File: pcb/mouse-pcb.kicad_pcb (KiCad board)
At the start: 2 copper layers, 47.6 x 42.5 mm, 1 part, among them U1 PAW3395-T6QU

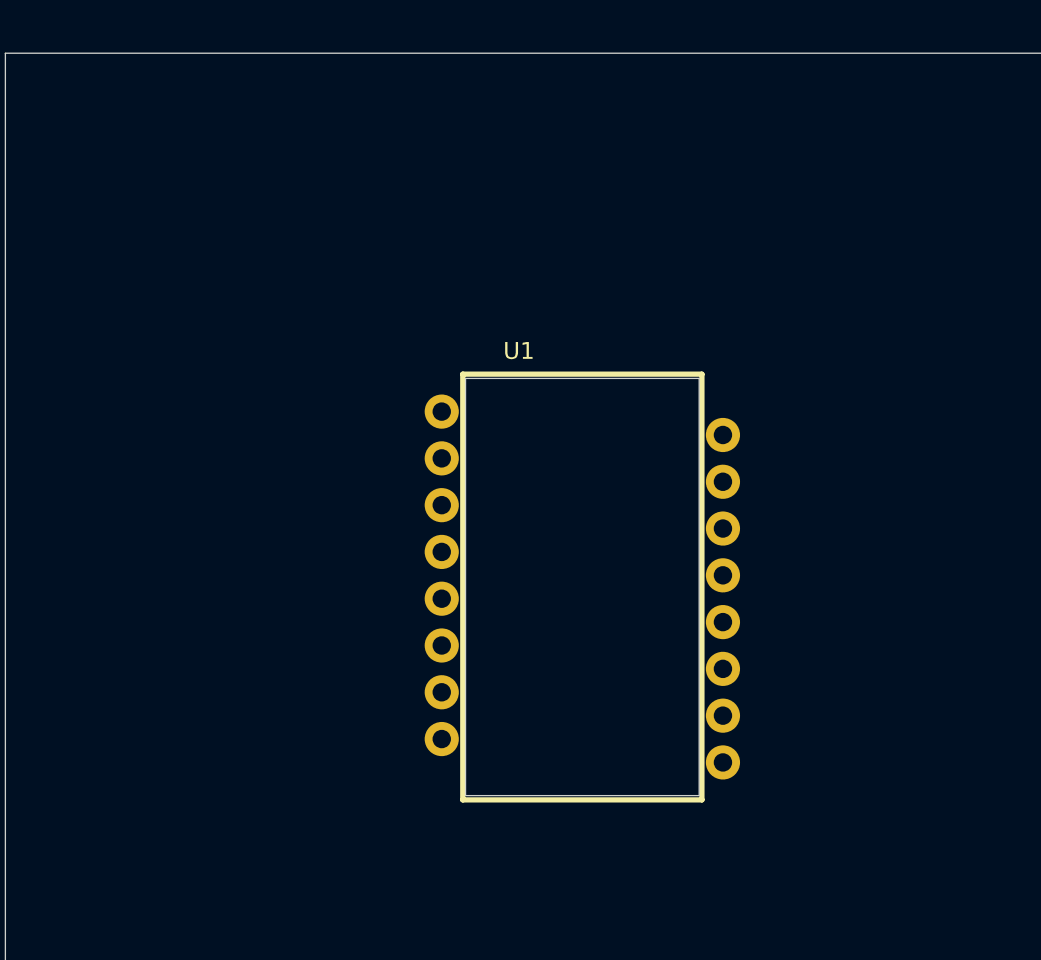
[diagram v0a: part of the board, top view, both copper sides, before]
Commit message: feat: add new library for the mouse
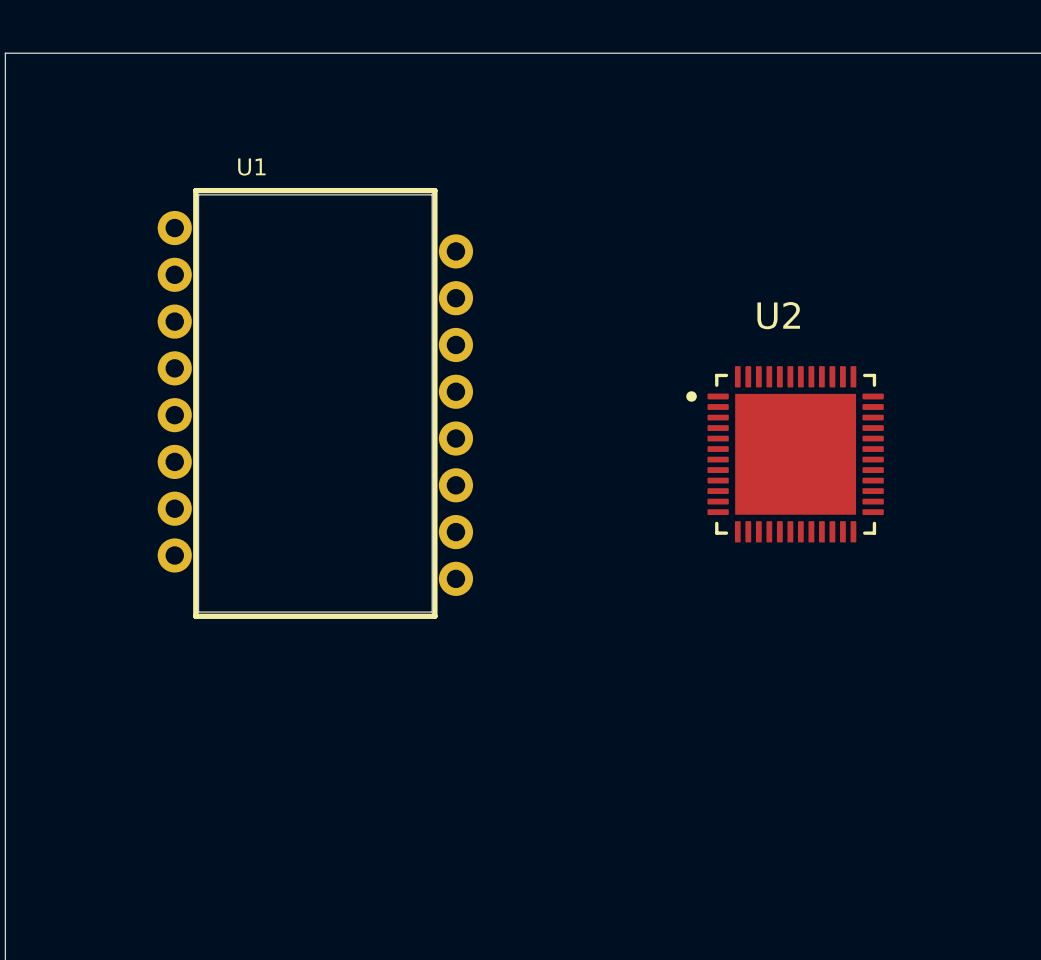
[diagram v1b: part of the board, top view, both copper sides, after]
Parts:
- added U2: NRF54L15-QFAA-R, mouse_library:QFN40P600X600X90-49N, F.Cu at (89.8, 44.8)
- U1: footprint paw3395:paw3395 -> mouse_library:paw3395
- moved U1 12.3 mm to (71.5, 42.9)
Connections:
- U1 pad 3: unconnected-(U1-GND-Pad3) -> GND
- U1 pad 4: unconnected-(U1-VDD-Pad4) -> +3V3
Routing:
- added copper zone on In2.Cu, net +3V3
- added copper zone on In1.Cu, net GND
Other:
- copper layers 2 -> 4

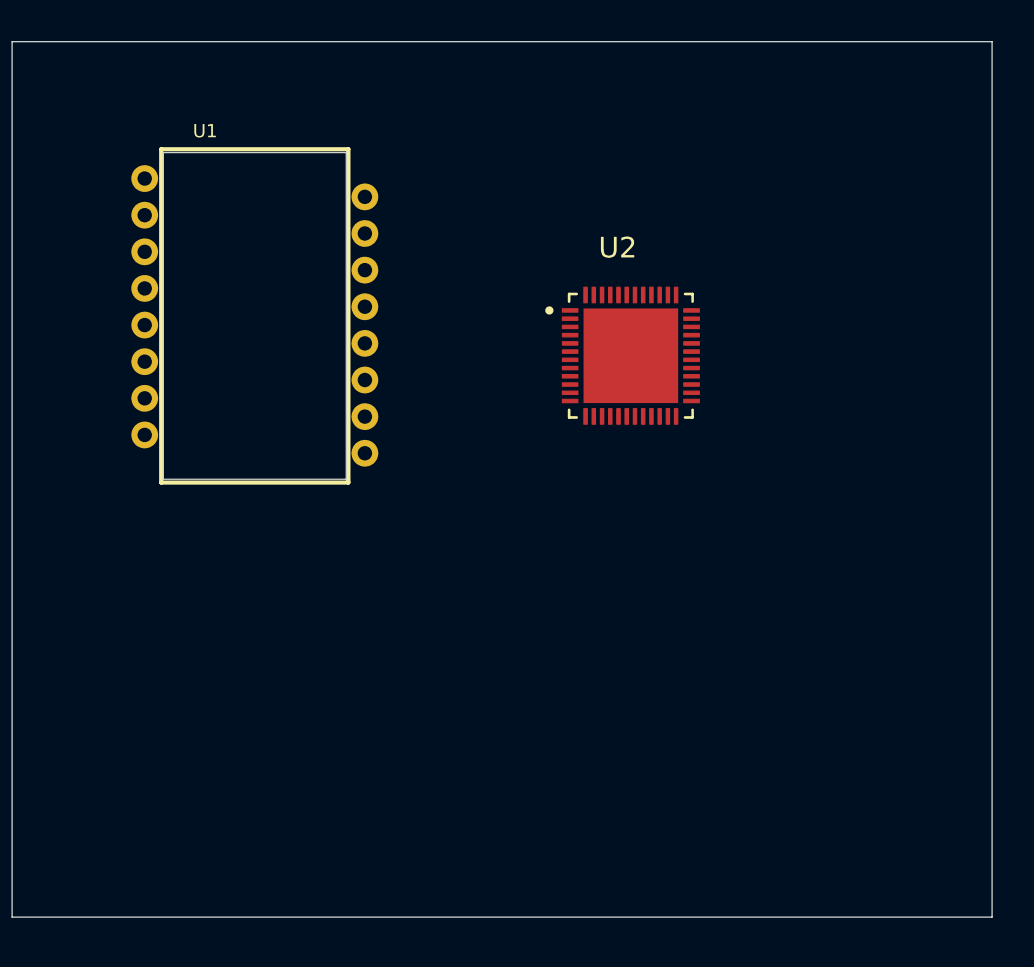
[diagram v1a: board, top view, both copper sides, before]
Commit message: feat: add more components to the library
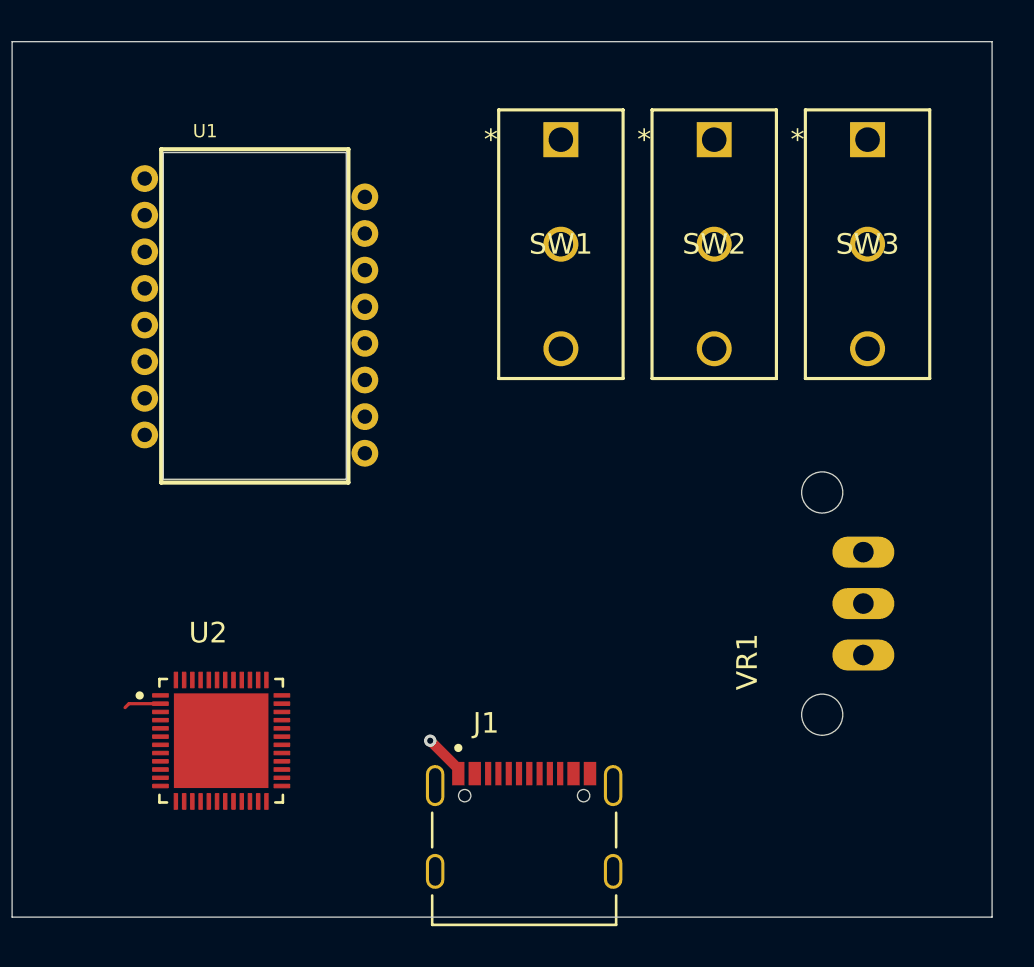
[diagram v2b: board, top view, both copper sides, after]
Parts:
- added J1: TYPE-C-31-M-12, mouse_library:HRO_TYPE-C-31-M-12, F.Cu at (84.6, 69.8)
- added SW1: D2FC-F-7N20M, mouse_library:SW_D2FC_OMR, F.Cu at (86.4, 34.3)
- added SW2: D2FC-F-7N20M, mouse_library:SW_D2FC_OMR, F.Cu at (93.8, 34.3)
- added SW3: D2FC-F-7N20M, mouse_library:SW_D2FC_OMR, F.Cu at (101.3, 34.3)
- added VR1: EC10E1220501, mouse_library:TRIM_EC10E1220501, F.Cu at (101.1, 56.8)
- moved U2 27.3 mm to (69.8, 63.5)
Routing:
- net GND: track 0.00 -> 2.17 mm, vias 0 -> 1
- net unconnected-(U2-P1.01/XL2-Pad2): track 0.00 -> 1.80 mm

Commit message: feat: adding all the passive for mouse
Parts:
- added C1: 4.7uF, Capacitor_SMD:C_0805_2012Metric_Pad1.18x1.45mm_HandSolder, F.Cu at (77.8, 57.6)
- added C2: 100nF, Capacitor_SMD:C_0805_2012Metric_Pad1.18x1.45mm_HandSolder, F.Cu at (80.8, 57.6)
- added C3: 10uF, Capacitor_SMD:C_0805_2012Metric_Pad1.18x1.45mm_HandSolder, F.Cu at (83.8, 57.6)
- added C4: 100nF, Capacitor_SMD:C_0805_2012Metric_Pad1.18x1.45mm_HandSolder, F.Cu at (86.9, 57.6)
- added C5: 100nF, Capacitor_SMD:C_0805_2012Metric_Pad1.18x1.45mm_HandSolder, F.Cu at (89.9, 57.6)
- added C6: 10uF, Capacitor_SMD:C_0805_2012Metric_Pad1.18x1.45mm_HandSolder, F.Cu at (92.9, 57.6)
- added C7: 33uF, Capacitor_SMD:C_0805_2012Metric_Pad1.18x1.45mm_HandSolder, F.Cu at (95.9, 57.6)
- added R1: 10K, Resistor_SMD:R_0805_2012Metric_Pad1.20x1.40mm_HandSolder, F.Cu at (77.8, 52.8)
- added R2: 5R6, Resistor_SMD:R_0805_2012Metric_Pad1.20x1.40mm_HandSolder, F.Cu at (80.7, 52.8)
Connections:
- U1 pad 10: unconnected-(U1-SCLK-Pad10) -> SCLK
- U1 pad 11: unconnected-(U1-MOSI-Pad11) -> MOSI
- U1 pad 12: unconnected-(U1-MISO-Pad12) -> MISO
- U1 pad 13: unconnected-(U1-NCS-Pad13) -> NCS
- U1 pad 14: unconnected-(U1-NRESET-Pad14) -> NRESET
- U1 pad 15: unconnected-(U1-LED_P-Pad15) -> Net-(U1-LED_P)
- U1 pad 4: +3V3 -> +1V9
- U1 pad 5: unconnected-(U1-VDDREG-Pad5) -> VDDREG
- U1 pad 7: unconnected-(U1-VDDIO-Pad7) -> +3V3
- U1 pad 8: unconnected-(U1-GNDIO-Pad8) -> GND
- U1 pad 9: unconnected-(U1-MOTION-Pad9) -> MOTION

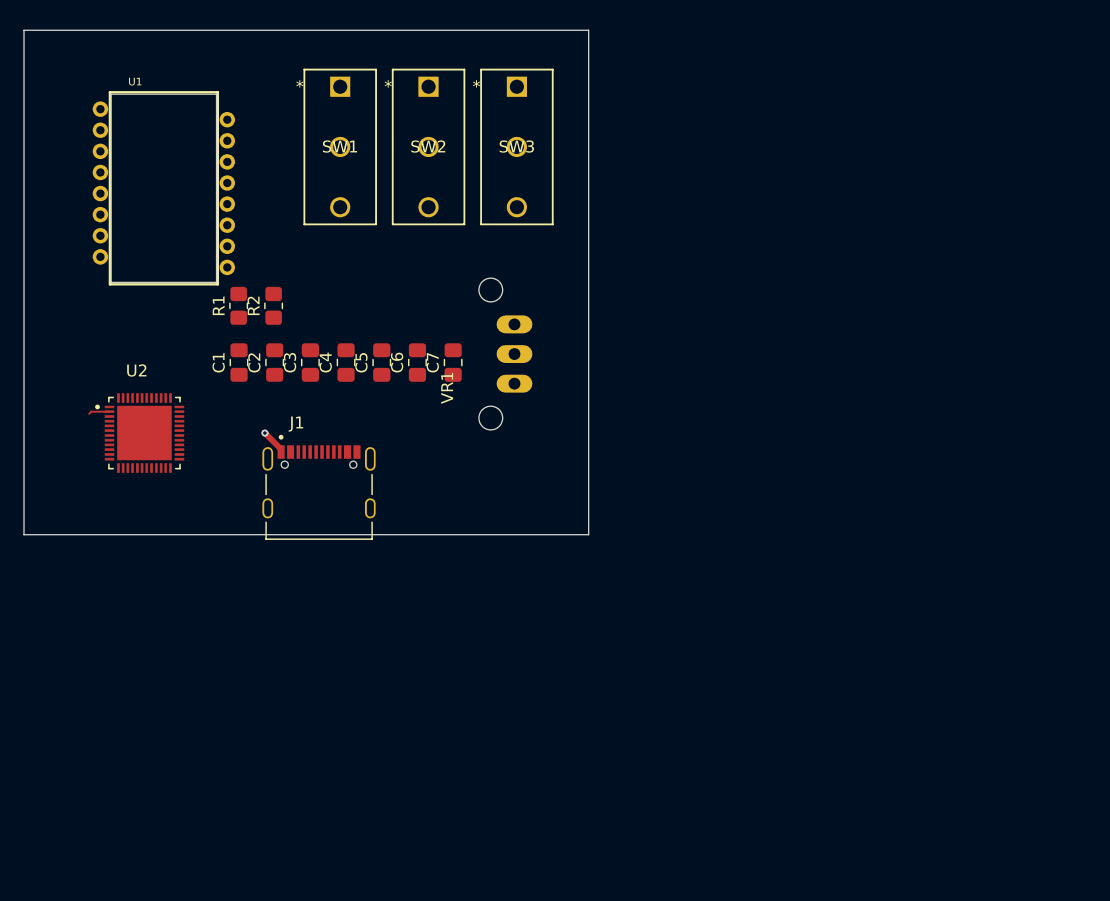
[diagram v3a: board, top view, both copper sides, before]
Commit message: feat: all connections for the mouse sensor done
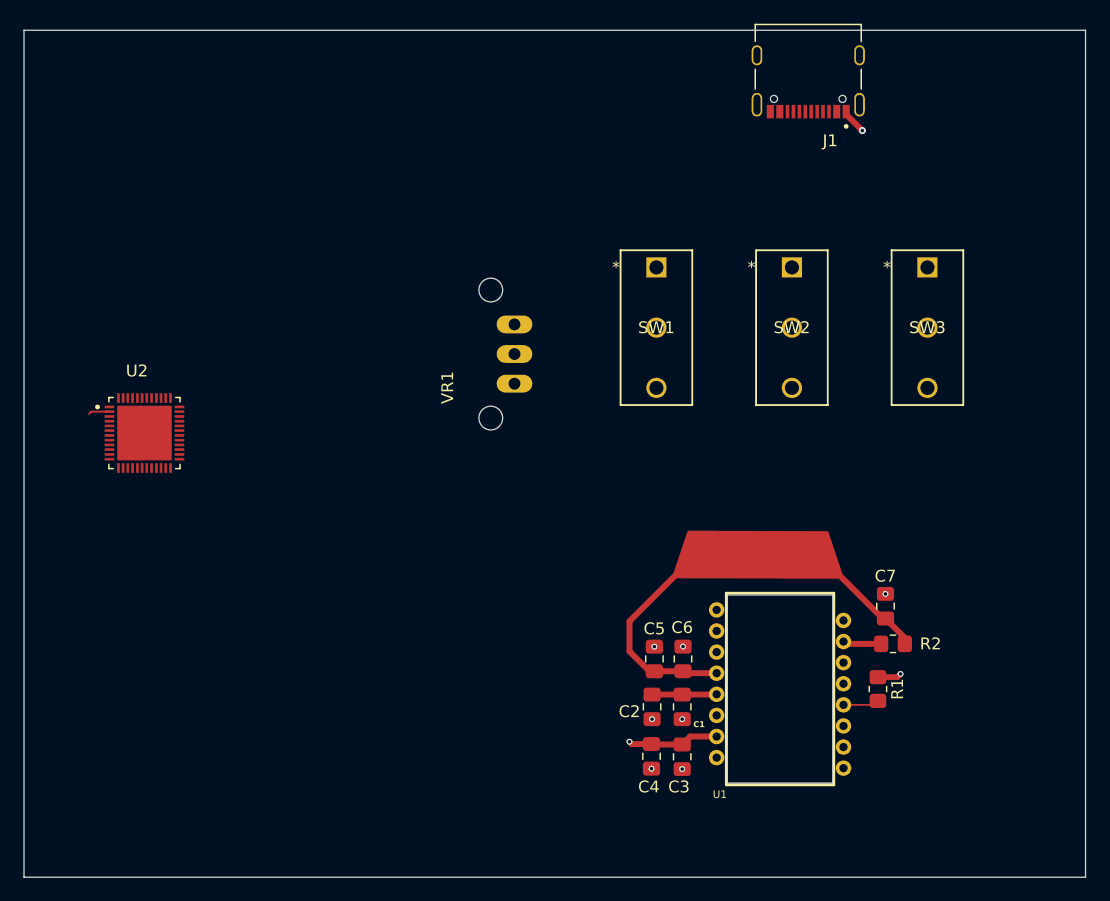
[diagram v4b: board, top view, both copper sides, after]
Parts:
- moved U1 67.0 mm to (123.5, 85.1)
- moved R1 62.9 mm to (131.7, 85.1), turned to -90 degrees
- moved R2 59.5 mm to (133.0, 81.3), turned to 0 degrees
- moved J1 56.2 mm to (125.8, 31.6), turned to 180 degrees
- moved C1 47.3 mm to (115.2, 86.6), turned to -90 degrees
- moved C3 45.7 mm to (115.2, 90.8), turned to -90 degrees
- moved C2 43.1 mm to (112.7, 86.6), turned to -90 degrees
- moved C4 42.0 mm to (112.6, 90.8), turned to -90 degrees
- moved C7 41.9 mm to (132.3, 78.1)
- moved SW3 37.8 mm to (135.9, 49.5)
- moved SW2 34.2 mm to (124.5, 49.5)
- moved C5 34.0 mm to (112.9, 82.5)
- moved C6 33.6 mm to (115.3, 82.5)
- moved SW1 30.7 mm to (113.0, 49.5)
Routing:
- net +1V9: track 0.00 -> 38.7 mm
- net +3V3: track 0.00 -> 9.74 mm, vias 0 -> 2
- net VDDREG: track 0.00 -> 5.07 mm
- net Net-(U1-LED_P): track 0.00 -> 3.26 mm
- net MISO: track 0.00 -> 3.04 mm
- net GND: track 2.17 -> 1.93 mm, vias 1 -> 8
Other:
- board size 47.6 x 42.5 mm -> 89.5 x 71.4 mm

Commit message: fix: improve the tracks and zones
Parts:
- moved R2 0.91 mm to (132.1, 81.3)
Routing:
- net GND: track 1.93 -> 12.9 mm
- net NCS: track 0.00 -> 8.53 mm
- net NRESET: track 0.00 -> 8.48 mm
- net MOSI: track 0.00 -> 8.37 mm
- net MISO: track 3.04 -> 11.3 mm
- net SCLK: track 0.00 -> 8.16 mm
- net MOTION: track 0.00 -> 8.03 mm
- net Net-(U1-LED_P): track 3.26 -> 2.52 mm
- added copper zone on F.Cu, net +1V9
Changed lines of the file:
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@@
 	(footprint "Resistor_SMD:R_0805_2012Metric_Pad1.20x1.40mm_HandSolder"
 		(layer "F.Cu")
-		(at 132.985 81.28)
+		(at 132.08 81.28)
 		(descr "Resistor SMD 0805 (2012 Metric), square (rectangular) end terminal, IPC-7351 nominal with elongated pad for handsoldering. (Body size source: IPC-SM-782 page 72, https://www.pcb-3d.com/wordpress/wp-content/uploads/ipc-sm-782a_amendment_1_and_2.pdf), generated with kicad-footprint-generator")
 		(tags "resistor handsolder")
@@
 		)
 	)
-	(gr_poly
-		(pts
-			(xy 114.466074 75.64799) (xy 115.736074 71.83799) (xy 127.445762 71.876696) (xy 128.715762 75.686696)
-		)
-		(stroke
-			(width 0.2)
-			(type solid)
-		)
-		(fill yes)
-		(layer "F.Cu")
-		(net 5)
-	)
 	(gr_rect
 		(start 59.69 29.5275)
@@
 	)
 	(segment
+		(start 116.205 87.63)
+		(end 115.205 87.63)
+		(width 0.5)
+		(layer "F.Cu")
+		(net 1)
+	)
+	(segment
+		(start 116.84 86.995)
+		(end 116.205 87.63)
+		(width 0.5)
+		(layer "F.Cu")
+		(net 1)
+	)
+	(segment
 		(start 129.035562 36.622277)
 		(end 130.400561 37.987276)
@@
 		(net 1)
 	)
+	(segment
+		(start 132.35 77.0675)
+		(end 132.35 75.565)
+		(width 0.5)
+		(layer "F.Cu")
+		(net 1)
+	)
+	(segment
+		(start 112.665 87.63)
+		(end 111.125 87.63)
+		(width 0.5)
+		(layer "F.Cu")
+		(net 1)
+	)
+	(segment
+		(start 115.205 91.8425)
+		(end 115.205 93.345)
+		(width 0.5)
+		(layer "F.Cu")
+		(net 1)
+	)
+	(segment
+		(start 115.274487 81.5125)
+		(end 115.274487 80.01)
+		(width 0.5)
+		(layer "F.Cu")
+		(net 1)
+	)
+	(segment
+		(start 112.617219 91.8058)
+		(end 112.617219 93.345)
+		(width 0.5)
+		(layer "F.Cu")
+		(net 1)
+	)
+	(segment
+		(start 112.860614 81.5125)
+		(end 112.860614 80.01)
+		(width 0.5)
+		(layer "F.Cu")
+		(net 1)
+	)
 	(via
-		(at 115.274487 81.5125)
+		(at 115.274487 80.01)
 		(size 0.5)
 		(drill 0.3)
@@
 	)
 	(via
-		(at 112.665 87.63)
+		(at 111.125 87.63)
 		(size 0.5)
 		(drill 0.3)
@@
 	)
 	(via
-		(at 115.205 87.63)
+		(at 116.84 86.995)
 		(size 0.5)
 		(drill 0.3)
@@
 	)
 	(via
-		(at 112.617219 91.8058)
+		(at 112.617219 93.345)
 		(size 0.5)
 		(drill 0.3)
@@
 	)
 	(via
-		(at 132.35 77.0675)
+		(at 132.35 75.565)
 		(size 0.5)
 		(drill 0.3)
@@
 	)
 	(via
-		(at 115.205 91.8425)
+		(at 115.205 93.345)
 		(size 0.5)
 		(drill 0.3)
@@
 	)
 	(via
-		(at 112.860614 81.5125)
+		(at 112.860614 80.01)
 		(size 0.5)
 		(drill 0.3)
@@
 	)
 	(segment
-		(start 133.985 81.28)
-		(end 133.985 80.7775)
-		(width 0.5)
-		(layer "F.Cu")
-		(net 5)
-	)
-	(segment
 		(start 132.35 79.1425)
 		(end 132.1175 79.1425)
@@
 	)
 	(segment
+		(start 133.08 81.28)
+		(end 133.08 79.8725)
+		(width 0.5)
+		(layer "F.Cu")
+		(net 5)
+	)
+	(segment
+		(start 133.08 79.8725)
+		(end 132.35 79.1425)
+		(width 0.5)
+		(layer "F.Cu")
+		(net 5)
+	)
+	(segment
 		(start 110.76 79.375)
 		(end 110.76 81.915)
-		(width 0.5)
-		(layer "F.Cu")
-		(net 5)
-	)
-	(segment
-		(start 133.985 80.7775)
-		(end 132.35 79.1425)
 		(width 0.5)
 		(layer "F.Cu")
@@
 	(segment
 		(start 128.81 86.425)
+		(end 137.095 86.425)
+		(width 0.156)
+		(layer "F.Cu")
+		(net 6)
+	)
+	(segment
+		(start 128.81 86.425)
 		(end 131.38 86.425)
 		(width 0.156)
 		(layer "F.Cu")
 		(net 6)
+	)
+	(segment
+		(start 129.005 81.28)
+		(end 128.81 81.085)
+		(width 0.5)
+		(layer "F.Cu")
+		(net 7)
 	)
 	(segment
@@
 	)
 	(segment
-		(start 129.175 81.28)
-		(end 131.985 81.28)
+		(start 131.08 81.28)
+		(end 129.005 81.28)
 		(width 0.5)
 		(layer "F.Cu")
@@
 	)
 	(segment
-		(start 129.005 81.28)
-		(end 128.81 81.085)
+		(start 128.81 89.985)
+		(end 136.975 89.985)
 		(width 0.156)
 		(layer "F.Cu")
-		(net 7)
+		(net 9)
+	)
+	(segment
+		(start 136.845 82.865)
+		(end 137.16 82.55)
+		(width 0.156)
+		(layer "F.Cu")
+		(net 11)
+	)
+	(segment
+		(start 128.81 82.865)
+		(end 136.845 82.865)
+		(width 0.156)
+		(layer "F.Cu")
+		(net 11)
+	)
+	(segment
+		(start 128.81 88.205)
+		(end 137.1 88.205)
+		(width 0.156)
+		(layer "F.Cu")
+		(net 13)
+	)
+	(segment
+		(start 137.1 88.205)
+		(end 137.16 88.265)
+		(width 0.156)
+		(layer "F.Cu")
+		(net 13)
+	)
+	(segment
+		(start 129.255 85.09)
+		(end 137.16 85.09)
+		(width 0.156)
+		(layer "F.Cu")
+		(net 14)
+	)
+	(segment
+		(start 128.81 84.645)
+		(end 129.255 85.09)
+		(width 0.156)
+		(layer "F.Cu")
+		(net 14)
+	)
+	(segment
+		(start 128.81 91.765)
+		(end 136.835 91.765)
+		(width 0.156)
+		(layer "F.Cu")
+		(net 15)
 	)
 	(segment
@@
 		(layer "F.Cu")
 		(net 30)
+	)
+	(zone
+		(net 5)
+		(net_name "+1V9")
+		(layer "F.Cu")
+		(hatch edge 0.5)
+		(priority 2)
+		(connect_pads yes
+			(clearance 0.5)
+		)
+		(min_thickness 0.25)
+		(filled_areas_thickness no)
+		(fill yes
+			(thermal_gap 0.5)
+			(thermal_bridge_width 0.5)
+		)
+		(polygon
+			(pts
+				(xy 135.89 82.55) (xy 135.89 71.755) (xy 109.855 71.755) (xy 109.855 84.455) (xy 115.84 84.455)
+				(xy 115.84 82.55)
+			)
+		)
 	)
 	(zone
@@
 		(layer "In1.Cu")
 		(hatch edge 0.5)
-		(connect_pads
+		(connect_pads yes
 			(clearance 0.5)
 		)
@@
 		(hatch edge 0.5)
 		(priority 1)
-		(connect_pads
+		(connect_pads yes
 			(clearance 0.5)
 		)
